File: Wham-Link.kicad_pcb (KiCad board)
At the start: 4 copper layers, 70 x 30 mm, 63 parts, among them J2 Conn_02x05_Counter_Clockwise, J3 Conn_01x09_Pin, Q1 2SC4617R, Q3 UMH3N, SW2 SKRPACE010, SW3 SKRPACE010, U1 LAN8720A-CP-TR, U2 AMS1117-3.3, U3 CH340C, U4 ESP32-WROOM-32UE, X1 ECS-2520MV-250-CN-TR

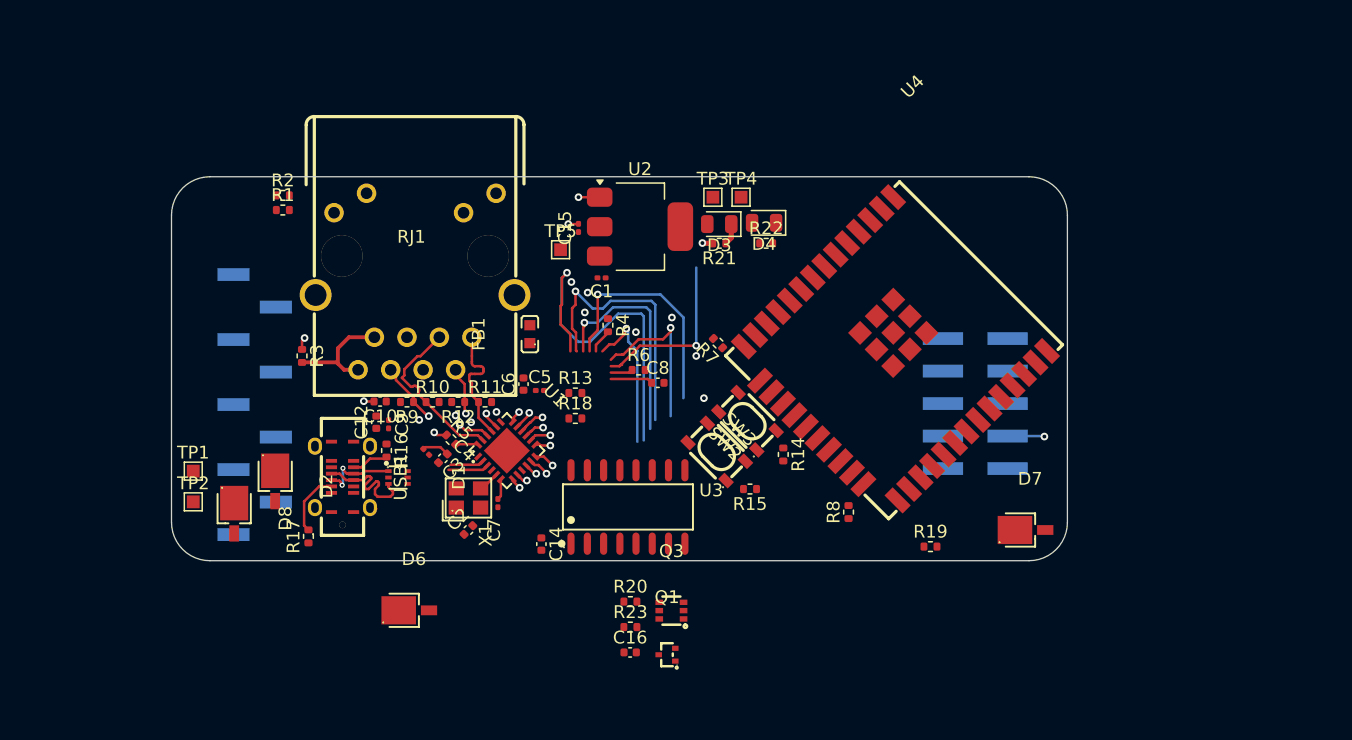
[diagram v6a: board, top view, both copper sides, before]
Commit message: Progress on PCB layout draft
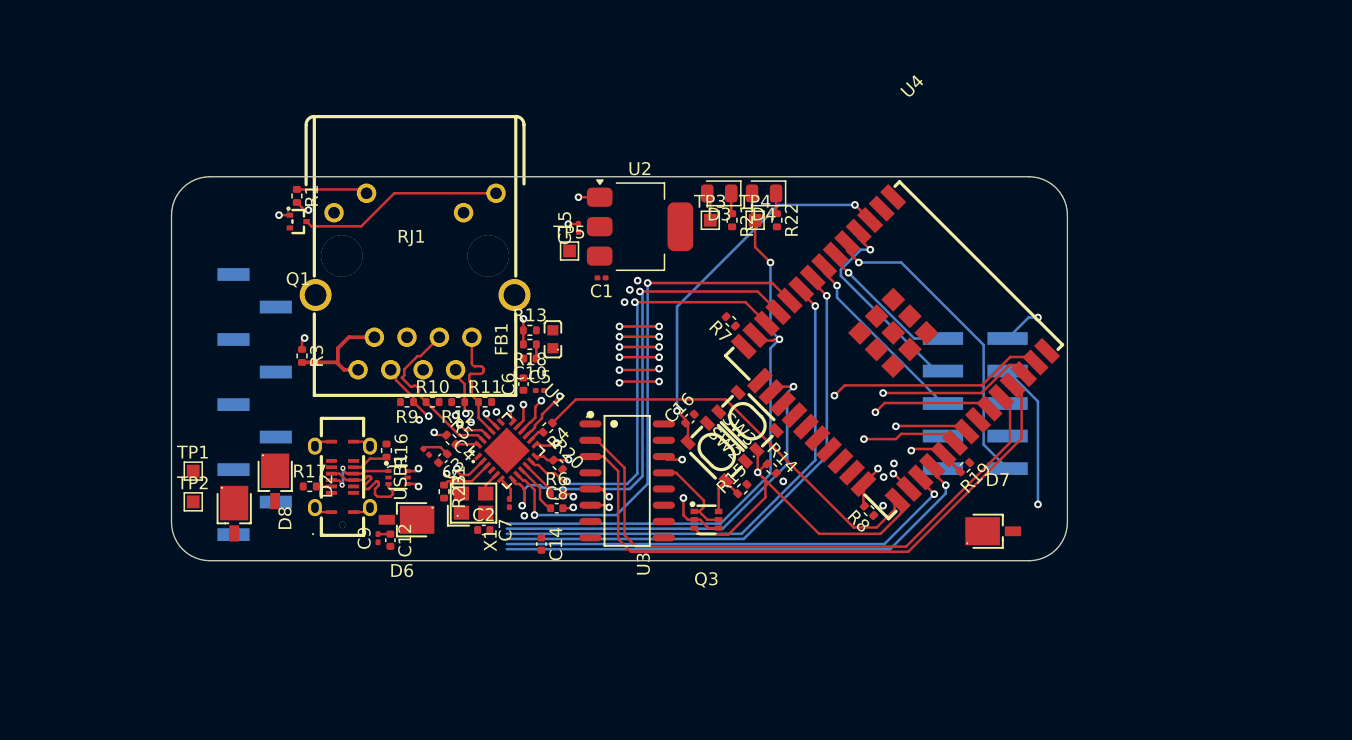
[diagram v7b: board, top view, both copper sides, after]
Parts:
- removed R2: 332R, Resistor_SMD:R_0402_1005Metric
- moved Q1 44.4 mm to (122.9, 88.5), turned to 180 degrees
- moved C16 18.9 mm to (153.5, 103.9), turned to 45 degrees
- moved R23 18.0 mm to (134.3, 109.6), turned to -90 degrees
- moved C8 12.6 mm to (143.1, 110.9)
- moved C10 12.2 mm to (141.0, 99.2)
- moved R20 12.1 mm to (143.2, 107.5), turned to -45 degrees
- moved R6 11.6 mm to (143.1, 109.8)
- moved C12 9.29 mm to (130.1, 113.4), turned to -90 degrees
- moved R4 9.28 mm to (142.4, 104.6), turned to -135 degrees
- moved C9 8.94 mm to (129.1, 113.2), turned to 90 degrees
- moved Q3 7.61 mm to (154.8, 111.8), turned to 180 degrees
- moved D6 7.14 mm to (131.0, 111.8), turned to 180 degrees
- moved R18 6.79 mm to (141.0, 98.1), turned to 180 degrees
- moved R19 6.76 mm to (175.0, 107.7), turned to -135 degrees
- moved R13 6.05 mm to (141.0, 97.0)
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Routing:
- net BOOT: track 0.00 -> 59.5 mm, vias 0 -> 1
- net TXD0: track 0.00 -> 48.0 mm
- net GP14: track 0.00 -> 47.4 mm, vias 0 -> 2
- net RXD0: track 0.00 -> 46.5 mm
- net GP32: track 0.00 -> 42.1 mm, vias 0 -> 1
- net GP33: track 0.00 -> 40.3 mm, vias 0 -> 1
- net IO25: track 0.93 -> 41.0 mm, vias 1 -> 2
- net IO26: track 0.89 -> 39.9 mm, vias 1 -> 2
- net GP17: track 0.00 -> 38.7 mm, vias 0 -> 1
- net GP16: track 0.00 -> 36.8 mm, vias 0 -> 1
- net EN: track 0.00 -> 33.9 mm, vias 0 -> 2
- net /LED1: track 3.17 -> 35.6 mm, vias 0 -> 2
- net GP13: track 0.00 -> 32.2 mm, vias 0 -> 1
- net /LED2: track 2.63 -> 34.7 mm, vias 0 -> 2
- net IO23: track 13.2 -> 44.4 mm, vias 2 -> 4
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- removed copper zone on In1.Cu, net (none)

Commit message: re-layout
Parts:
- removed TP5: TestPoint_Small, TestPoint:TestPoint_Pad_1.0x1.0mm
- C1, C15, C4, C5, C7, C9: footprint Capacitor_SMD:C_0201_0603Metric -> Capacitor_SMD:C_0603_1608Metric
- moved C12 40.3 mm to (155.6, 82.2), turned to 0 degrees
- moved C9 39.9 mm to (155.4, 83.2), turned to 180 degrees
- moved R17 37.0 mm to (148.6, 81.8), turned to 180 degrees
- moved D6 35.4 mm to (155.2, 86.0), turned to 90 degrees
- moved USB1 33.3 mm to (149.0, 84.1), turned to 0 degrees
- moved R16 28.2 mm to (150.9, 87.6), turned to 180 degrees
- moved Q3 28.1 mm to (158.8, 84.0)
- moved R15 27.2 mm to (159.2, 82.2), turned to 180 degrees
- moved D1 27.2 mm to (149.0, 88.4), turned to 180 degrees
- moved C15 26.7 mm to (160.1, 110.9), turned to 0 degrees
- moved D3 26.3 mm to (166.8, 110.2), turned to 0 degrees
- moved SW3 25.0 mm to (163.6, 82.8), turned to 180 degrees
- moved C16 25.0 mm to (167.1, 82.9), turned to 90 degrees
- moved SW2 24.7 mm to (170.5, 82.8), turned to 180 degrees
- moved C14 24.6 mm to (145.4, 89.4), turned to 180 degrees
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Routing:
- net +3V3: track 6.18 -> 81.6 mm, vias 0 -> 2
- net /VDD1A: track 2.14 -> 64.3 mm, vias 0 -> 2
- net TXD0: track 48.0 -> 0.00 mm
- net RXD0: track 46.5 -> 0.00 mm
- net +5V: track 0.00 -> 45.9 mm
- net IO5: track 40.6 -> 3.78 mm, vias 4 -> 1
- net GP17: track 38.7 -> 68.9 mm
- net /LED2: track 34.7 -> 6.72 mm, vias 2 -> 0
- net /LED1: track 35.6 -> 9.92 mm, vias 2 -> 0
- net EN: track 33.9 -> 8.83 mm, vias 2 -> 0
- net GPI39: track 24.7 -> 0.00 mm, vias 1 -> 0
- net GP16: track 36.8 -> 60.7 mm
- net GP13: track 32.2 -> 55.0 mm
- net Net-(D2-A): track 0.00 -> 20.9 mm, vias 0 -> 1
- net GP32: track 42.1 -> 61.7 mm
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- added copper zone on B.Cu, net GND
- added copper zone on F.Cu, net GND
- added copper zone on In2.Cu, net Net-(D6-A)
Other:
- board size 70 x 30 mm -> 70 x 35 mm
